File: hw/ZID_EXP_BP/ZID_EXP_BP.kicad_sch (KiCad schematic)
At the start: 14 parts, among them J10 USB-C PWR ONLY

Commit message: Add TP for open CPLD pins
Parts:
- removed J?: Conn_02x03_Odd_Even, symbol Connector_Generic:Conn_02x03_Odd_Even
- added J? (x2): Conn_02x05_2.54mm, symbol Connector_Generic:Conn_02x05_Row_Letter_First
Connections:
- net +5V: now also J?.b1 (Pin_b1), J?.b1 (Pin_b1)
- net GND: now also J?.a1 (Pin_a1), J?.a1 (Pin_a1), J?.a2 (Pin_a2), J?.a2 (Pin_a2), J?.a3 (Pin_a3), J?.a3 (Pin_a3), J?.a4 (Pin_a4), J?.a4 (Pin_a4), J?.a5 (Pin_a5), J?.a5 (Pin_a5)
- net MODINT-: now also J?.b5 (Pin_b5)
- net SBC_I0: now also J?.b2 (Pin_b2)
- net SBC_I1: now also J?.b3 (Pin_b3)
- net SBC_O0: now also J?.b2 (Pin_b2)
- net SBC_O1: now also J?.b3 (Pin_b3)
- new net SBC_I2: J?.b4 (Pin_b4)
- new net SBC_O2: J?.b4 (Pin_b4)
- new net SBS_O3: J?.b5 (Pin_b5)

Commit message: 8 output bits on RP. 10k PU for most. TVS.
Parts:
- added H? (x4): MountingHole, symbol Mechanical:MountingHole
- added JP? (x3): Jumper_2_Small_Open, symbol Jumper:Jumper_2_Small_Open
- added OP? (x5): AES-Option_A-B, Connector_PinHeader_2.54mm:PinHeader_1x03_P2.54mm_Vertical, symbol AES_Library:AES-Option_A-B
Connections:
- net INT-: now also OP?.1 (A)
- net MODINT-: now also OP?.2 (C)
- net RX: now also OP?.1 (A), OP?.3 (B)
- net RX2: now also OP?.1 (A), OP?.3 (B)
- net SBC_I0: now also OP?.2 (C)
- net SBC_I1: now also JP?.2 (B)
- net SBC_I2: now also OP?.2 (C)
- net SBC_O0: now also OP?.2 (C)
- net SBC_O1: now also JP?.2 (B)
- net SBC_O2: now also OP?.2 (C)
- net TX: now also OP?.1 (A), OP?.3 (B)
- net TX2: now also OP?.1 (A), OP?.3 (B)
- net USR4: now also JP?.1 (A)
- net USR6: now also JP?.1 (A)
- net USR7: now also JP?.1 (A)
- net ZIRQ1: now also OP?.3 (B)
- net SBS_O3 renamed SBC_O3
- net SBC_O3: now also JP?.2 (B)
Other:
- moved on the sheet: J?

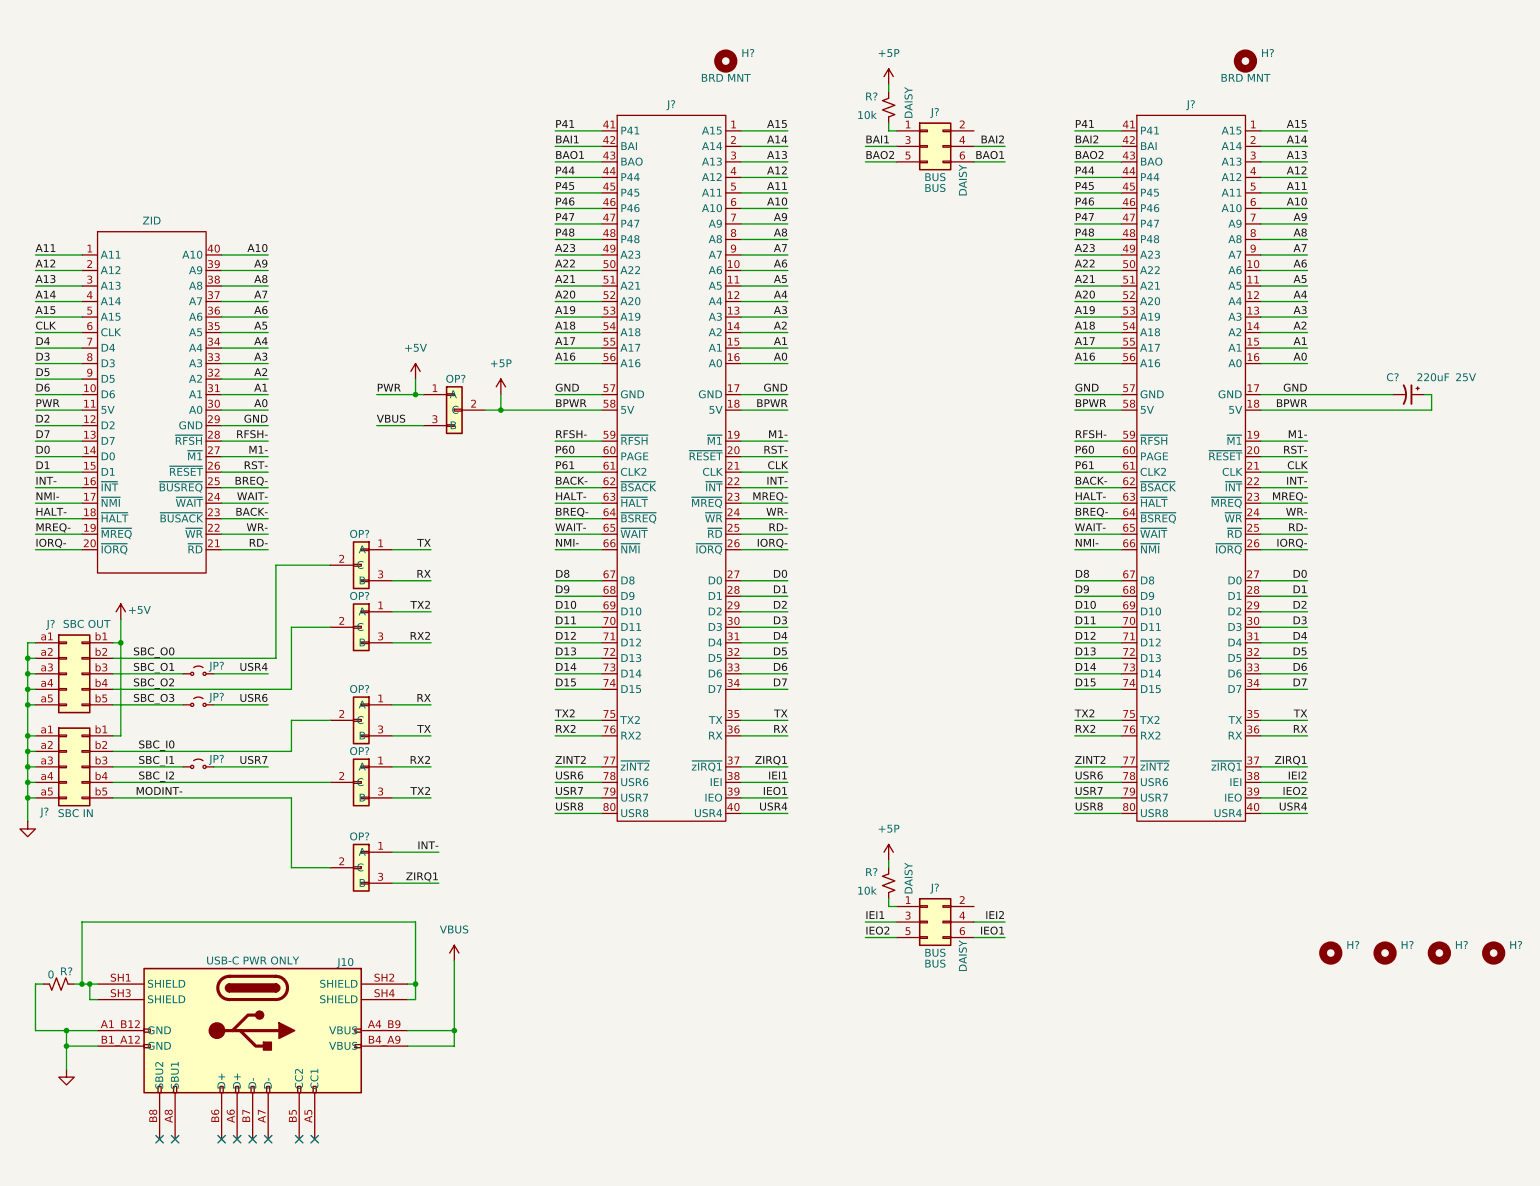
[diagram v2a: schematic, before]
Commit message: Exp-BP: Add display
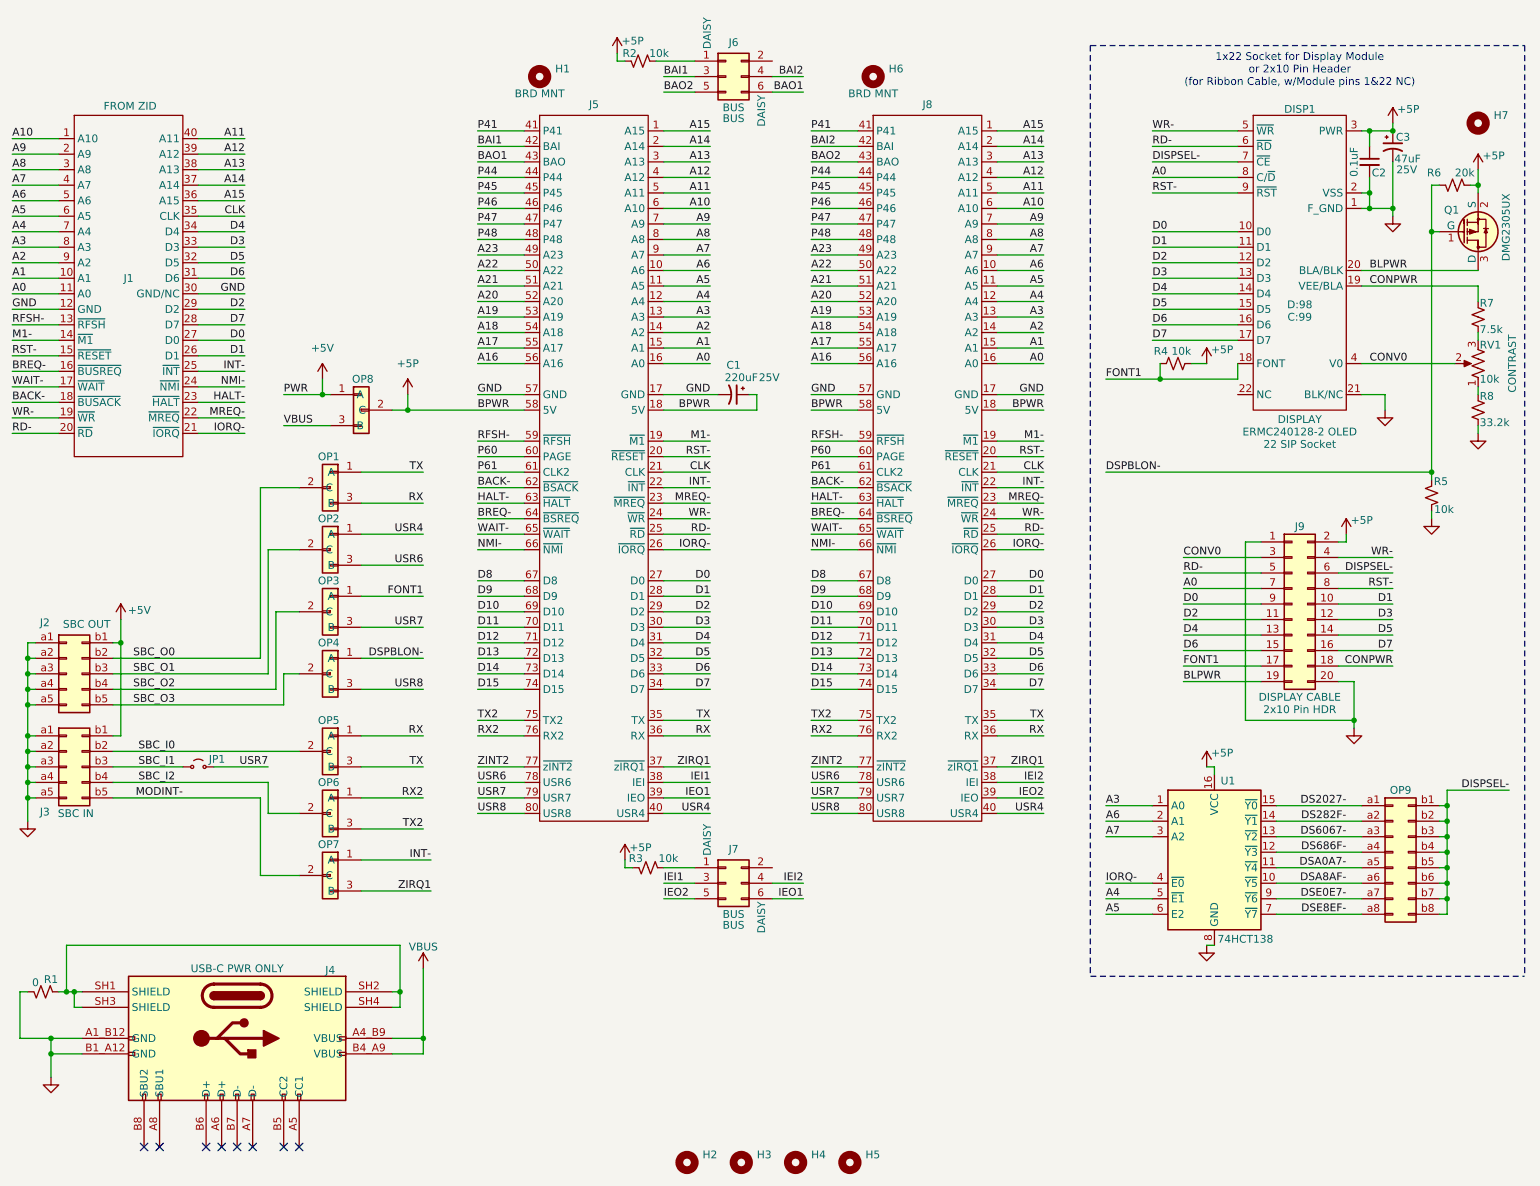
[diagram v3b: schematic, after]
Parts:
- removed J?: ZID, Connector_PinHeader_2.00mm:PinHeader_2x20_P2.00mm_Vertical, symbol AES_Library:Z80-Target-AES
- removed JP? (x2): Jumper_2_Small_Open, symbol Jumper:Jumper_2_Small_Open
- removed R? (x2): 10k, Resistor_SMD:R_0805_2012Metric_Pad1.20x1.40mm_HandSolder, symbol Device:R_Small_US
- added C2: 0.1uF, Capacitor_SMD:C_0603_1608Metric, symbol Device:C_Small
- added C3: 47uF, Capacitor_THT:CP_Radial_D4.0mm_P1.50mm, symbol Device:C_Polarized_Small_US
- added DISP1: DISPLAY, AES_Library:OLED-Disp-Socket-P2-8BitPI-AES, symbol AES_Library:Display_ERMC240128-2_OLED-AES
- added H7: MountingHole, symbol Mechanical:MountingHole
- added J1: FROM ZID, AES_Library:CviLux_CF25401D0-05-NH_FFC-FPC-AES, symbol AES_Library:Z80-Pod-AES
- added J9: HDR 2x10 Pin, Connector_PinHeader_2.54mm:PinHeader_2x10_P2.54mm_Vertical, symbol Connector_Generic:Conn_02x10_Odd_Even
- added OP3, OP4: AES-Option_A-B, Connector_PinHeader_2.54mm:PinHeader_1x03_P2.54mm_Vertical, symbol AES_Library:AES-Option_A-B
- added OP9: Conn_02x08_2mm, symbol Connector_Generic:Conn_02x08_Row_Letter_First
- added Q1: DMG2305UX, AES_Library:DMG2305-SOT-23-3-AES, symbol AES_Library:DMG2305UX-AES
- added R2, R3: 10k, Resistor_SMD:R_0805_2012Metric_Pad1.20x1.40mm_HandSolder, symbol Device:R_Small_US
- added R4, R5: 10k, Resistor_SMD:R_0805_2012Metric, symbol Device:R_Small_US
- added R6: 20k, Resistor_SMD:R_0805_2012Metric, symbol Device:R_Small_US
- added R7: 7.5k, Resistor_SMD:R_0805_2012Metric, symbol Device:R_Small_US
- added R8: 33.2k, Resistor_SMD:R_0805_2012Metric, symbol Device:R_Small_US
- added RV1: 10k, AES_Library:Pot-Molence-Amazon-PCB-AES, symbol Device:R_Potentiometer_US
- added U1: 74HCT138, symbol 74xx:74HCT138
- gave numbers to parts that had none: 21
- renumbered J10 to J4
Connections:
- net +5P: now also C2.1, C3.1, DISP1.3 (PWR), J9.2 (Pin_2), Q1.2 (S), R2.1, R3.1, R4.2, R6.1, U1.16 (VCC)
- net A0: now also DISP1.8 (C/~{D}), J1.11 (A0), J9.7 (Pin_7)
- net A1: now also J1.10 (A1)
- net A10: now also J1.1 (A10)
- net A11: now also J1.40 (A11)
- net A12: now also J1.39 (A12)
- net A13: now also J1.38 (A13)
- net A14: now also J1.37 (A14)
- net A15: now also J1.36 (A15)
- net A2: now also J1.9 (A2)
- net A3: now also J1.8 (A3), U1.1 (A0)
- net A4: now also J1.7 (A4), U1.5 (~{E1})
- net A5: now also J1.6 (A5), U1.6 (E2)
- net A6: now also J1.5 (A6), U1.2 (A1)
- net A7: now also J1.4 (A7), U1.3 (A2)
- net A8: now also J1.3 (A8)
- net A9: now also J1.2 (A9)
- net BACK-: now also J1.18 (~{BUSACK})
- net BREQ-: now also J1.16 (~{BUSREQ})
- net CLK: now also J1.35 (CLK)
- net D0: now also DISP1.10 (D0), J1.27 (D0), J9.9 (Pin_9)
- net D1: now also DISP1.11 (D1), J1.26 (D1), J9.10 (Pin_10)
- net D2: now also DISP1.12 (D2), J1.29 (D2), J9.11 (Pin_11)
- net D3: now also DISP1.13 (D3), J1.33 (D3), J9.12 (Pin_12)
- net D4: now also DISP1.14 (D4), J1.34 (D4), J9.13 (Pin_13)
- net D5: now also DISP1.15 (D5), J1.32 (D5), J9.14 (Pin_14)
- net D6: now also DISP1.16 (D6), J1.31 (D6), J9.15 (Pin_15)
- net D7: now also DISP1.17 (D7), J1.28 (D7), J9.16 (Pin_16)
- net GND: now also C2.2, C3.2, DISP1.1 (F_GND), DISP1.2 (VSS), DISP1.21 (BLK/NC), J1.12 (GND), J1.30 (GND/NC), J9.1 (Pin_1), J9.20 (Pin_20), R5.2, R8.2, U1.8 (GND)
- net HALT-: now also J1.23 (~{HALT})
- net INT-: now also J1.25 (~{INT})
- net IORQ-: now also J1.21 (~{IORQ}), U1.4 (~{E0})
- net M1-: now also J1.14 (~{M1})
- net MREQ-: now also J1.22 (~{MREQ})
- net NMI-: now also J1.24 (~{NMI})
- net RD-: now also DISP1.6 (~{RD}), J1.20 (~{RD}), J9.5 (Pin_5)
- net RFSH-: now also J1.13 (~{RFSH})
- net RST-: now also DISP1.9 (~{RST}), J1.15 (~{RESET}), J9.8 (Pin_8)
- net RX2: no longer OP2.3 (B)
- net SBC_O1: now also OP2.2 (C)
- net SBC_O2: now also OP3.2 (C); no longer OP2.2 (C)
- net SBC_O3: now also OP4.2 (C)
- net TX2: no longer OP2.1 (A)
- net USR4: now also OP2.1 (A)
- net USR6: now also OP2.3 (B)
- net USR7: now also OP3.3 (B)
- net USR8: now also OP4.3 (B)
- net WAIT-: now also J1.17 (~{WAIT})
- net WR-: now also DISP1.5 (~{WR}), J1.19 (~{WR}), J9.4 (Pin_4)
- net at J7.1 (Pin_1): now also R3.2
- net at J6.1 (Pin_1): now also R2.2
- new net: R7.2, RV1.3
- new net: R8.1, RV1.1
- new net BLPWR: DISP1.20 (BLA/BLK), J9.19 (Pin_19), Q1.3 (D)
- new net CONPWR: DISP1.19 (VEE/BLA), J9.18 (Pin_18), R7.1
- new net CONV0: DISP1.4 (V0), J9.3 (Pin_3), RV1.2
- new net DISPSEL-: DISP1.7 (~{CE}), J9.6 (Pin_6), OP9.b1 (Pin_b1), OP9.b2 (Pin_b2), OP9.b3 (Pin_b3), OP9.b4 (Pin_b4), OP9.b5 (Pin_b5), OP9.b6 (Pin_b6), OP9.b7 (Pin_b7), OP9.b8 (Pin_b8)
- new net DS2027-: OP9.a1 (Pin_a1), U1.15 (~{Y0})
- new net DS282F-: OP9.a2 (Pin_a2), U1.14 (~{Y1})
- new net DS6067-: OP9.a3 (Pin_a3), U1.13 (~{Y2})
- new net DS686F-: OP9.a4 (Pin_a4), U1.12 (~{Y3})
- new net DSA0A7-: OP9.a5 (Pin_a5), U1.11 (~{Y4})
- new net DSA8AF-: OP9.a6 (Pin_a6), U1.10 (~{Y5})
- new net DSE0E7-: OP9.a7 (Pin_a7), U1.9 (~{Y6})
- new net DSE8EF-: OP9.a8 (Pin_a8), U1.7 (~{Y7})
- new net DSPBLON-: OP4.1 (A), Q1.1 (G), R5.1, R6.2
- new net FONT1: DISP1.18 (FONT), J9.17 (Pin_17), OP3.1 (A), R4.1
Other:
- note added: "1x22 Socket for Display Module or 2x10 Pin Header (for Ribbon Cable, w/Module pins 1&22 NC)"
- moved on the sheet: C1, H1, H2, H3, H4, H5, H6, J4, J5, J6, J7, J8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
